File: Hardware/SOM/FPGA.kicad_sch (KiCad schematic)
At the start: 57 parts, among them U1 LFE5UM5G-85F

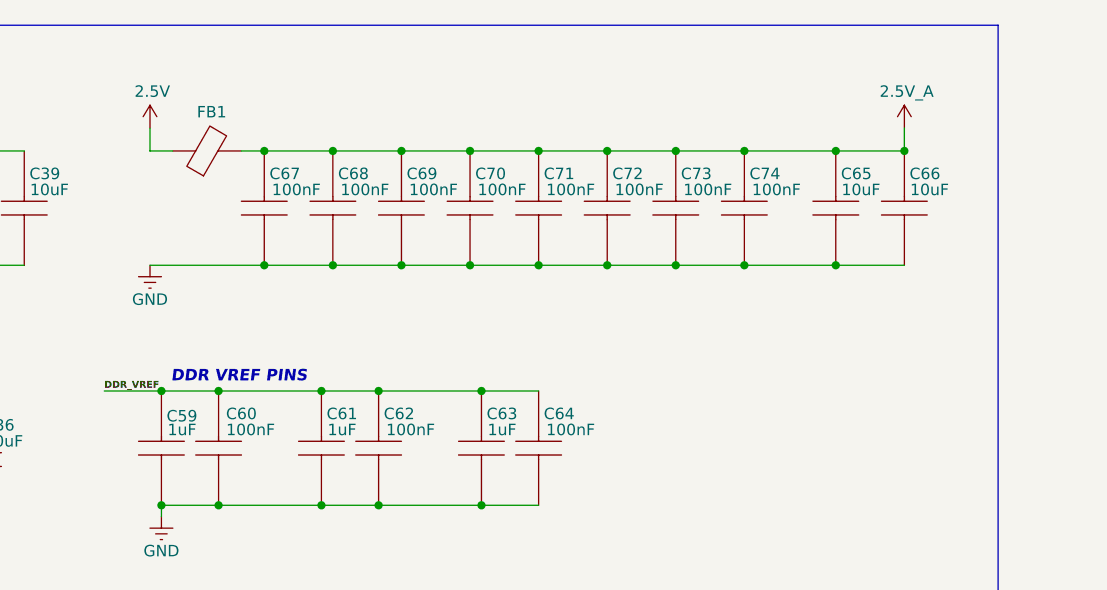
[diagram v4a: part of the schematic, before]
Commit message: SOM: power supply update
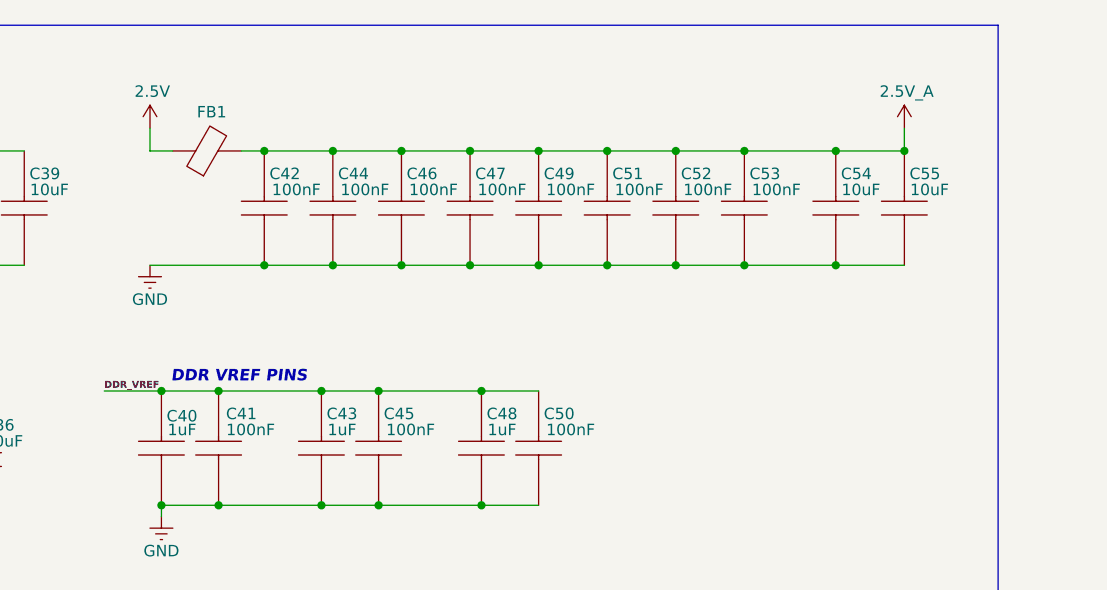
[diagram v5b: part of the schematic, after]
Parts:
- renumbered C59 to C40, C60 to C41, C67 to C42, C61 to C43, C68 to C44, C62 to C45, C69 to C46, C70 to C47, C63 to C48, C71 to C49, C64 to C50, C72 to C51, C73 to C52, C74 to C53, C65 to C54, C66 to C55
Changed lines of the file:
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@@
 		(on_board yes)
 		(dnp no)
-		(property "Reference" "#PWR049"
+		(property "Reference" "#PWR020"
 			(at 132.08 217.17 0)
 			(effects
@@
 			(project "LFE5UM5G-85F_SOM"
 				(path "/de32abb0-ff3b-4c67-a91a-eed08140b1b2/c389ef9b-5ef6-4b55-8e02-1ff1b5373fc6"
-					(reference "#PWR049")
+					(reference "#PWR020")
 					(unit 1)
 				)
@@
 		(on_board yes)
 		(dnp no)
-		(property "Reference" "C69"
+		(property "Reference" "C46"
 			(at 161.036 153.67 90)
 			(effects
@@
 			(project "LFE5UM5G-85F_SOM"
 				(path "/de32abb0-ff3b-4c67-a91a-eed08140b1b2/c389ef9b-5ef6-4b55-8e02-1ff1b5373fc6"
-					(reference "C69")
+					(reference "C46")
 					(unit 1)
 				)
@@
 		(on_board yes)
 		(dnp no)
-		(property "Reference" "#PWR045"
+		(property "Reference" "#PWR023"
 			(at 172.72 241.3 0)
 			(effects
@@
 			(project "LFE5UM5G-85F_SOM"
 				(path "/de32abb0-ff3b-4c67-a91a-eed08140b1b2/c389ef9b-5ef6-4b55-8e02-1ff1b5373fc6"
-					(reference "#PWR045")
+					(reference "#PWR023")
 					(unit 1)
 				)
@@
 		(on_board yes)
 		(dnp no)
-		(property "Reference" "#PWR046"
+		(property "Reference" "#PWR017"
 			(at 130.81 152.4 0)
 			(effects
@@
 			(project "LFE5UM5G-85F_SOM"
 				(path "/de32abb0-ff3b-4c67-a91a-eed08140b1b2/c389ef9b-5ef6-4b55-8e02-1ff1b5373fc6"
-					(reference "#PWR046")
+					(reference "#PWR017")
 					(unit 1)
 				)
@@
 		(on_board yes)
 		(dnp no)
-		(property "Reference" "C70"
+		(property "Reference" "C47"
 			(at 168.656 153.67 90)
 			(effects
@@
 			(project "LFE5UM5G-85F_SOM"
 				(path "/de32abb0-ff3b-4c67-a91a-eed08140b1b2/c389ef9b-5ef6-4b55-8e02-1ff1b5373fc6"
-					(reference "C70")
+					(reference "C47")
 					(unit 1)
 				)
@@
 		(on_board yes)
 		(dnp no)
-		(property "Reference" "C63"
+		(property "Reference" "C48"
 			(at 169.926 180.34 90)
 			(effects
@@
 			(project "LFE5UM5G-85F_SOM"
 				(path "/de32abb0-ff3b-4c67-a91a-eed08140b1b2/c389ef9b-5ef6-4b55-8e02-1ff1b5373fc6"
-					(reference "C63")
+					(reference "C48")
 					(unit 1)
 				)
@@
 		(on_board yes)
 		(dnp no)
-		(property "Reference" "C68"
+		(property "Reference" "C44"
 			(at 153.416 153.67 90)
 			(effects
@@
 			(project "LFE5UM5G-85F_SOM"
 				(path "/de32abb0-ff3b-4c67-a91a-eed08140b1b2/c389ef9b-5ef6-4b55-8e02-1ff1b5373fc6"
-					(reference "C68")
+					(reference "C44")
 					(unit 1)
 				)
@@
 		(on_board yes)
 		(dnp no)
-		(property "Reference" "C59"
+		(property "Reference" "C40"
 			(at 134.366 180.594 90)
 			(effects
@@
 			(project "LFE5UM5G-85F_SOM"
 				(path "/de32abb0-ff3b-4c67-a91a-eed08140b1b2/c389ef9b-5ef6-4b55-8e02-1ff1b5373fc6"
-					(reference "C59")
+					(reference "C40")
 					(unit 1)
 				)
@@
 		(on_board yes)
 		(dnp no)
-		(property "Reference" "C67"
+		(property "Reference" "C42"
 			(at 145.796 153.67 90)
 			(effects
@@
 			(project "LFE5UM5G-85F_SOM"
 				(path "/de32abb0-ff3b-4c67-a91a-eed08140b1b2/c389ef9b-5ef6-4b55-8e02-1ff1b5373fc6"
-					(reference "C67")
+					(reference "C42")
 					(unit 1)
 				)
@@
 		(on_board yes)
 		(dnp no)
-		(property "Reference" "C61"
+		(property "Reference" "C43"
 			(at 152.146 180.34 90)
 			(effects
@@
 			(project "LFE5UM5G-85F_SOM"
 				(path "/de32abb0-ff3b-4c67-a91a-eed08140b1b2/c389ef9b-5ef6-4b55-8e02-1ff1b5373fc6"
-					(reference "C61")
+					(reference "C43")
 					(unit 1)
 				)
@@
 		(on_board yes)
 		(dnp no)
-		(property "Reference" "#PWR019"
+		(property "Reference" "#PWR024"
 			(at 190.5 30.48 0)
 			(effects
@@
 			(project "LFE5UM5G-85F_SOM"
 				(path "/de32abb0-ff3b-4c67-a91a-eed08140b1b2/c389ef9b-5ef6-4b55-8e02-1ff1b5373fc6"
-					(reference "#PWR019")
+					(reference "#PWR024")
 					(unit 1)
 				)
@@
 		(on_board yes)
 		(dnp no)
-		(property "Reference" "#PWR017"
+		(property "Reference" "#PWR022"
 			(at 144.78 30.48 0)
 			(effects
@@
 			(project "LFE5UM5G-85F_SOM"
 				(path "/de32abb0-ff3b-4c67-a91a-eed08140b1b2/c389ef9b-5ef6-4b55-8e02-1ff1b5373fc6"
-					(reference "#PWR017")
+					(reference "#PWR022")
 					(unit 1)
 				)
@@
 		(on_board yes)
 		(dnp no)
-		(property "Reference" "C66"
+		(property "Reference" "C55"
 			(at 216.916 153.67 90)
 			(effects
@@
 			(project "LFE5UM5G-85F_SOM"
 				(path "/de32abb0-ff3b-4c67-a91a-eed08140b1b2/c389ef9b-5ef6-4b55-8e02-1ff1b5373fc6"
-					(reference "C66")
+					(reference "C55")
 					(unit 1)
 				)
@@
 		(on_board yes)
 		(dnp no)
-		(property "Reference" "#PWR06"
+		(property "Reference" "#PWR07"
 			(at 26.67 257.81 0)
 			(effects
@@
 			(project "LFE5UM5G-85F_SOM"
 				(path "/de32abb0-ff3b-4c67-a91a-eed08140b1b2/c389ef9b-5ef6-4b55-8e02-1ff1b5373fc6"
-					(reference "#PWR06")
+					(reference "#PWR07")
 					(unit 1)
 				)
@@
 		(on_board yes)
 		(dnp no)
-		(property "Reference" "C73"
+		(property "Reference" "C52"
 			(at 191.516 153.67 90)
 			(effects
@@
 			(project "LFE5UM5G-85F_SOM"
 				(path "/de32abb0-ff3b-4c67-a91a-eed08140b1b2/c389ef9b-5ef6-4b55-8e02-1ff1b5373fc6"
-					(reference "C73")
+					(reference "C52")
 					(unit 1)
 				)
@@
 		(on_board yes)
 		(dnp no)
-		(property "Reference" "C60"
+		(property "Reference" "C41"
 			(at 140.97 180.34 90)
 			(effects
@@
 			(project "LFE5UM5G-85F_SOM"
 				(path "/de32abb0-ff3b-4c67-a91a-eed08140b1b2/c389ef9b-5ef6-4b55-8e02-1ff1b5373fc6"
-					(reference "C60")
+					(reference "C41")
 					(unit 1)
 				)
@@
 		(on_board yes)
 		(dnp no)
-		(property "Reference" "#PWR043"
+		(property "Reference" "#PWR026"
 			(at 236.22 31.75 0)
 			(effects
@@
 			(project "LFE5UM5G-85F_SOM"
 				(path "/de32abb0-ff3b-4c67-a91a-eed08140b1b2/c389ef9b-5ef6-4b55-8e02-1ff1b5373fc6"
-					(reference "#PWR043")
+					(reference "#PWR026")
 					(unit 1)
 				)
@@
 		(on_board yes)
 		(dnp no)
-		(property "Reference" "#PWR047"
+		(property "Reference" "#PWR018"
 			(at 130.81 170.18 0)
 			(effects
@@
 			(project "LFE5UM5G-85F_SOM"
 				(path "/de32abb0-ff3b-4c67-a91a-eed08140b1b2/c389ef9b-5ef6-4b55-8e02-1ff1b5373fc6"
-					(reference "#PWR047")
+					(reference "#PWR018")
 					(unit 1)
 				)
@@
 		(on_board yes)
 		(dnp no)
-		(property "Reference" "#PWR022"
+		(property "Reference" "#PWR027"
 			(at 327.66 35.56 0)
 			(effects
@@
 			(project "LFE5UM5G-85F_SOM"
 				(path "/de32abb0-ff3b-4c67-a91a-eed08140b1b2/c389ef9b-5ef6-4b55-8e02-1ff1b5373fc6"
-					(reference "#PWR022")
+					(reference "#PWR027")
 					(unit 1)
 				)
@@
 		(on_board yes)
 		(dnp no)
-		(property "Reference" "C62"
+		(property "Reference" "C45"
 			(at 158.496 180.34 90)
 			(effects
@@
 			(project "LFE5UM5G-85F_SOM"
 				(path "/de32abb0-ff3b-4c67-a91a-eed08140b1b2/c389ef9b-5ef6-4b55-8e02-1ff1b5373fc6"
-					(reference "C62")
+					(reference "C45")
 					(unit 1)
 				)
@@
 		(on_board yes)
 		(dnp no)
-		(property "Reference" "C71"
+		(property "Reference" "C49"
 			(at 176.276 153.67 90)
 			(effects
@@
 			(project "LFE5UM5G-85F_SOM"
 				(path "/de32abb0-ff3b-4c67-a91a-eed08140b1b2/c389ef9b-5ef6-4b55-8e02-1ff1b5373fc6"
-					(reference "C71")
+					(reference "C49")
 					(unit 1)
 				)
@@
 		(on_board yes)
 		(dnp no)
-		(property "Reference" "C72"
+		(property "Reference" "C51"
 			(at 183.896 153.67 90)
 			(effects
@@
 			(project "LFE5UM5G-85F_SOM"
 				(path "/de32abb0-ff3b-4c67-a91a-eed08140b1b2/c389ef9b-5ef6-4b55-8e02-1ff1b5373fc6"
-					(reference "C72")
+					(reference "C51")
 					(unit 1)
 				)
@@
 		(on_board yes)
 		(dnp no)
-		(property "Reference" "#PWR044"
+		(property "Reference" "#PWR019"
 			(at 132.08 198.12 0)
 			(effects
@@
 			(project "LFE5UM5G-85F_SOM"
 				(path "/de32abb0-ff3b-4c67-a91a-eed08140b1b2/c389ef9b-5ef6-4b55-8e02-1ff1b5373fc6"
-					(reference "#PWR044")
+					(reference "#PWR019")
 					(unit 1)
 				)
@@
 		(on_board yes)
 		(dnp no)
-		(property "Reference" "C65"
+		(property "Reference" "C54"
 			(at 209.296 153.67 90)
 			(effects
@@
 			(project "LFE5UM5G-85F_SOM"
 				(path "/de32abb0-ff3b-4c67-a91a-eed08140b1b2/c389ef9b-5ef6-4b55-8e02-1ff1b5373fc6"
-					(reference "C65")
+					(reference "C54")
 					(unit 1)
 				)
@@
 		(on_board yes)
 		(dnp no)
-		(property "Reference" "C64"
+		(property "Reference" "C50"
 			(at 176.276 180.34 90)
 			(effects
@@
 			(project "LFE5UM5G-85F_SOM"
 				(path "/de32abb0-ff3b-4c67-a91a-eed08140b1b2/c389ef9b-5ef6-4b55-8e02-1ff1b5373fc6"
-					(reference "C64")
+					(reference "C50")
 					(unit 1)
 				)
@@
 		(on_board yes)
 		(dnp no)
-		(property "Reference" "#PWR018"
+		(property "Reference" "#PWR021"
 			(at 132.08 237.49 0)
 			(effects
@@
 			(project "LFE5UM5G-85F_SOM"
 				(path "/de32abb0-ff3b-4c67-a91a-eed08140b1b2/c389ef9b-5ef6-4b55-8e02-1ff1b5373fc6"
-					(reference "#PWR018")
+					(reference "#PWR021")
 					(unit 1)
 				)
@@
 		(on_board yes)
 		(dnp no)
-		(property "Reference" "#PWR07"
+		(property "Reference" "#PWR06"
 			(at 26.67 238.76 0)
 			(effects
@@
 			(project "LFE5UM5G-85F_SOM"
 				(path "/de32abb0-ff3b-4c67-a91a-eed08140b1b2/c389ef9b-5ef6-4b55-8e02-1ff1b5373fc6"
-					(reference "#PWR07")
+					(reference "#PWR06")
 					(unit 1)
 				)
@@
 		(on_board yes)
 		(dnp no)
-		(property "Reference" "C74"
+		(property "Reference" "C53"
 			(at 199.136 153.67 90)
 			(effects
@@
 			(project "LFE5UM5G-85F_SOM"
 				(path "/de32abb0-ff3b-4c67-a91a-eed08140b1b2/c389ef9b-5ef6-4b55-8e02-1ff1b5373fc6"
-					(reference "C74")
+					(reference "C53")
 					(unit 1)
 				)
@@
 		(on_board yes)
 		(dnp no)
-		(property "Reference" "#PWR048"
+		(property "Reference" "#PWR025"
 			(at 214.63 152.4 0)
 			(effects
@@
 			(project "LFE5UM5G-85F_SOM"
 				(path "/de32abb0-ff3b-4c67-a91a-eed08140b1b2/c389ef9b-5ef6-4b55-8e02-1ff1b5373fc6"
-					(reference "#PWR048")
+					(reference "#PWR025")
 					(unit 1)
 				)

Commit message: SOM: Serdes power
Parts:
- added C100, C84, C88, C92, C96: 1uF, Capacitor_SMD:C_0402_1005Metric, symbol RA8M1:885012205092
- added C101, C102, C85, C86, C89, C90, C93, C94, C97, C98: 100nF, Capacitor_SMD:C_0402_1005Metric, symbol RA8M1:885012205092
- added C83, C87, C91, C95, C99: 10uF, Capacitor_SMD:C_0402_1005Metric, symbol RA8M1:885012205092
- added FB4, FB5, FB6, FB7, FB8, FB9: FerriteBead, Inductor_SMD:L_1206_3216Metric, symbol Device:FerriteBead
- C47, C52: value 100nF -> 1uF; MPN 885012205092 -> 885012105006
- C53: value 100nF -> 10uF; MPN 885012205092 -> 885012105020
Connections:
- net 1.2V: now also FB4.1, FB5.1, FB6.1, FB7.1, FB8.1, FB9.1
- net 1.5V: no longer U1.F11 (VCCIO1), U1.F12 (VCCIO1)
- net 2.5V_A: no longer C49.2, C51.2, C52.2, C53.2, U1.T15 (VCCA1), U1.T6 (VCCA0), U1.U15 (VCCA1), U1.U6 (VCCA0)
- net 3.3V: now also C15.2, C19.2, C24.2, U1.F11 (VCCIO1), U1.F12 (VCCIO1)
- net GND: now also C100.1, C101.1, C102.1, C83.1, C84.1, C85.1, C86.1, C87.1, C88.1, C89.1, C90.1, C91.1, C92.1, C93.1, C94.1, C95.1, C96.1, C97.1, C98.1, C99.1
- net VCCHTX1: now reaches U1.T10 (VCCHTX1_D0CH1), U1.T14 (VCCHTX1_D1CH1)
- net VCCHTX1: now also C91.2, C92.2, C93.2, C94.2, FB7.2
- net VCCHTX0: now reaches U1.T11 (VCCHTX0_D1CH0), U1.T7 (VCCHTX0_D0CH0)
- net VCCHTX0: now also C87.2, C88.2, C89.2, C90.2, FB6.2
- net VCC_SER_0: now reaches U1.T12 (VCCHRX0_D1CH0), U1.T8 (VCCHRX0_D0CH0)
- net VCC_SER_0: now also C95.2, C96.2, C97.2, C98.2, FB8.2
- net VCC_SER_1: now reaches U1.T13 (VCCHRX1_D1CH1), U1.T9 (VCCHRX1_D0CH1)
- net VCC_SER_1: now also C100.2, C101.2, C102.2, C99.2, FB9.2
- new net VCCA0: C49.2, C51.2, C52.2, C53.2, FB4.2, U1.T6 (VCCA0), U1.U6 (VCCA0)
- new net VCCA1: C83.2, C84.2, C85.2, C86.2, FB5.2, U1.T15 (VCCA1), U1.U15 (VCCA1)
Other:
- note added: "ANALOG"
- note added: "SERDES VCCA"
- note added: "SERDES VCCHTX"
- note added: "VCCA 0"
- note added: "VCCA 1"
- moved on the sheet: C40, C41, C42, C43, C44, C45, C46, C48, C50, C54, C55, FB1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

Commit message: SOM: layout update
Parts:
- renumbered C53 to C40, C87 to C41, C95 to C42, C52 to C43, C88 to C44, C96 to C45, C42 to C46, C49 to C47, C89 to C48, C97 to C49, C44 to C50, C90 to C52, C98 to C53, C46 to C54, C47 to C55, C83 to C56, C91 to C57, C99 to C58, C54 to C59, C84 to C60, C92 to C61, C100 to C62, C55 to C63, C85 to C64, C93 to C65, C101 to C66, C86 to C67, C94 to C68, C102 to C69, C40 to C70, C41 to C71, C43 to C72, C45 to C73, C48 to C74, C50 to C75, FB4 to FB1, FB6 to FB2, FB8 to FB3, FB1 to FB4, FB7 to FB6, FB9 to FB7
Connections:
- net DDR_CKE renamed DDR_CK_P
- net DDR_NCK renamed DDR_CK_N
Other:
- note removed: "DDR VREF pins"

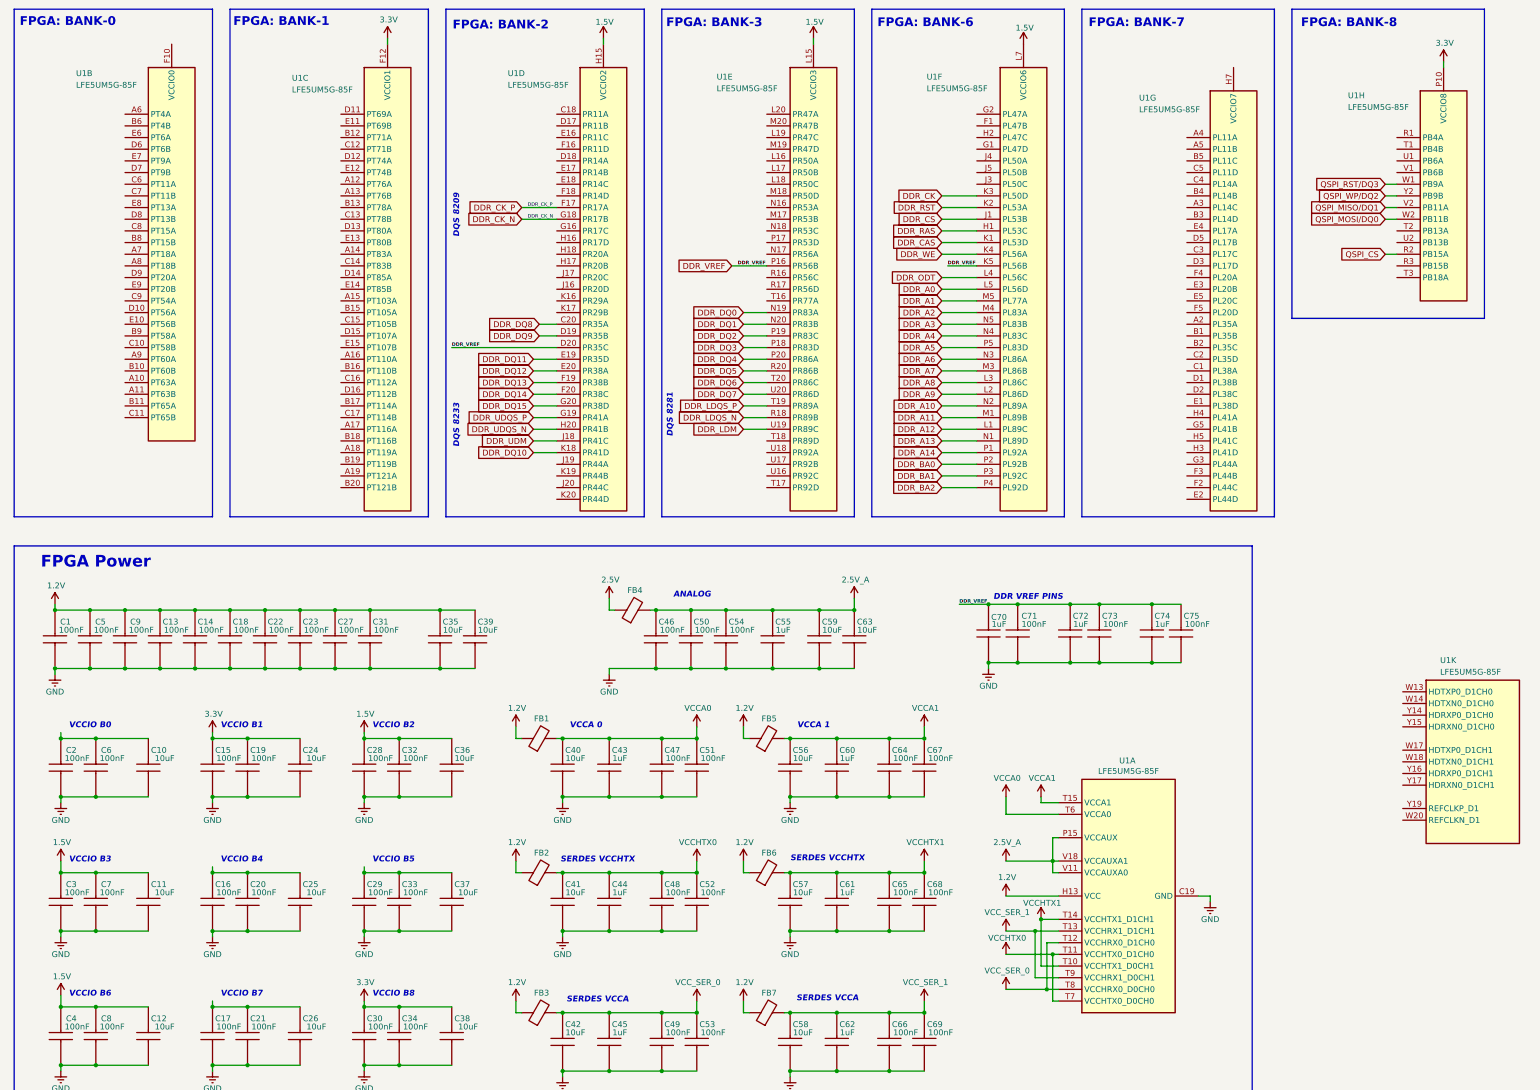
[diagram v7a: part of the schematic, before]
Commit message: SOM: layout update (QSPI+
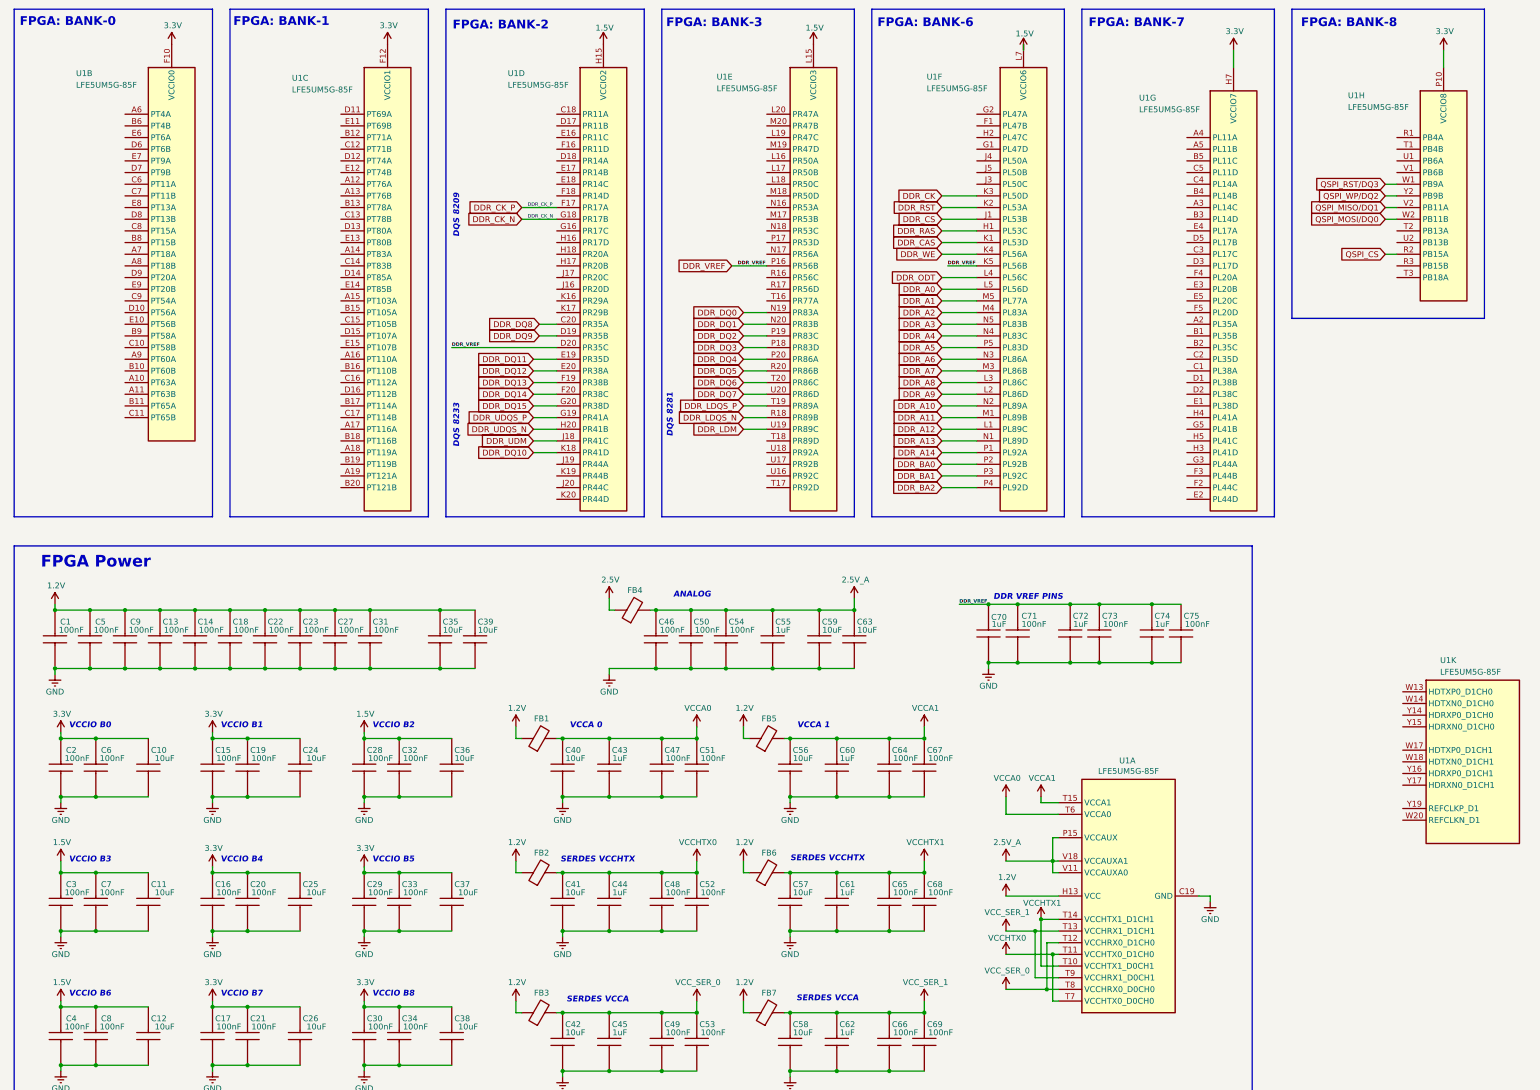
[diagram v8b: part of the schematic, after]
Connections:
- net 3.3V: now also C10.2, C16.2, C17.2, C2.2, C20.2, C21.2, C25.2, C26.2, C29.2, C33.2, C37.2, C6.2, U1.F10 (VCCIO0), U1.F9 (VCCIO0), U1.H6 (VCCIO7), U1.H7 (VCCIO7), U1.J6 (VCCIO7)
